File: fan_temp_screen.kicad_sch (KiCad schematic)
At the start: 19 parts, among them CN4 4P JST ZH, CN5 4P JST ZH, CN6 4P JST ZH

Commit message: Updated library name, updated and verified all footprints
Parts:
- C21: symbol EASYEDA2KICAD:C_100pF_C0G_0805 -> LiveAstra:C_100pF_C0G_0805
- CN4, CN5, CN6: symbol EASYEDA2KICAD:JST_ZH_4PIN_1A_50V -> LiveAstra:JST_ZH_4PIN_1A_50V
- R23, R24, R28, R30: symbol EASYEDA2KICAD:R_5k1Ohm_0402_62mW -> LiveAstra:R_5k1Ohm_0402_62mW
- R25, R26: symbol EASYEDA2KICAD:R_0Ohm_0805_125mW -> LiveAstra:R_0Ohm_0805_125mW
- R27: symbol EASYEDA2KICAD:R_10kOhm_0402_62mW -> LiveAstra:R_10kOhm_0402_62mW
- R29: symbol EASYEDA2KICAD:R_3k3Ohm_0805_125mW -> LiveAstra:R_3k3Ohm_0805_125mW
- TP48, TP49, TP50, TP51, TP52, TP53, TP54: symbol EASYEDA2KICAD:TestPoint_Thimble -> LiveAstra:TestPoint_Thimble
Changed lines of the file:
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@@
 	)
 	(symbol
-		(lib_id "EASYEDA2KICAD:TestPoint_Thimble")
+		(lib_id "LiveAstra:TestPoint_Thimble")
 		(at 187.96 96.52 0)
 		(unit 1)
@@
 	)
 	(symbol
-		(lib_id "EASYEDA2KICAD:TestPoint_Thimble")
+		(lib_id "LiveAstra:TestPoint_Thimble")
 		(at 142.24 40.64 0)
 		(unit 1)
@@
 	)
 	(symbol
-		(lib_id "EASYEDA2KICAD:R_0Ohm_0805_125mW")
+		(lib_id "LiveAstra:R_0Ohm_0805_125mW")
 		(at 167.64 48.26 0)
 		(unit 1)
@@
 	)
 	(symbol
-		(lib_id "EASYEDA2KICAD:JST_ZH_4PIN_1A_50V")
+		(lib_id "LiveAstra:JST_ZH_4PIN_1A_50V")
 		(at 106.68 152.4 180)
 		(unit 1)
@@
 	)
 	(symbol
-		(lib_id "EASYEDA2KICAD:R_5k1Ohm_0402_62mW")
+		(lib_id "LiveAstra:R_5k1Ohm_0402_62mW")
 		(at 124.46 86.36 90)
 		(unit 1)
@@
 	)
 	(symbol
-		(lib_id "EASYEDA2KICAD:+5V_IN")
+		(lib_id "LiveAstra:+5V_IN")
 		(at 132.08 60.96 0)
 		(unit 1)
@@
 	)
 	(symbol
-		(lib_id "EASYEDA2KICAD:C_100pF_C0G_0805")
+		(lib_id "LiveAstra:C_100pF_C0G_0805")
 		(at 215.9 55.88 90)
 		(unit 1)
@@
 	)
 	(symbol
-		(lib_id "EASYEDA2KICAD:R_10kOhm_0402_62mW")
+		(lib_id "LiveAstra:R_10kOhm_0402_62mW")
 		(at 177.8 40.64 90)
 		(unit 1)
@@
 	)
 	(symbol
-		(lib_id "EASYEDA2KICAD:TestPoint_Thimble")
+		(lib_id "LiveAstra:TestPoint_Thimble")
 		(at 144.78 142.24 0)
 		(unit 1)
@@
 	)
 	(symbol
-		(lib_id "EASYEDA2KICAD:TestPoint_Thimble")
+		(lib_id "LiveAstra:TestPoint_Thimble")
 		(at 157.48 35.56 0)
 		(unit 1)
@@
 	)
 	(symbol
-		(lib_id "EASYEDA2KICAD:R_5k1Ohm_0402_62mW")
+		(lib_id "LiveAstra:R_5k1Ohm_0402_62mW")
 		(at 203.2 142.24 90)
 		(unit 1)
@@
 	)
 	(symbol
-		(lib_id "EASYEDA2KICAD:TestPoint_Thimble")
+		(lib_id "LiveAstra:TestPoint_Thimble")
 		(at 228.6 45.72 0)
 		(unit 1)
@@
 	)
 	(symbol
-		(lib_id "EASYEDA2KICAD:TestPoint_Thimble")
+		(lib_id "LiveAstra:TestPoint_Thimble")
 		(at 149.86 91.44 0)
 		(unit 1)
@@
 	)
 	(symbol
-		(lib_id "EASYEDA2KICAD:R_3k3Ohm_0805_125mW")
+		(lib_id "LiveAstra:R_3k3Ohm_0805_125mW")
 		(at 205.74 48.26 0)
 		(unit 1)
@@
 	)
 	(symbol
-		(lib_id "EASYEDA2KICAD:JST_ZH_4PIN_1A_50V")
+		(lib_id "LiveAstra:JST_ZH_4PIN_1A_50V")
 		(at 106.68 101.6 180)
 		(unit 1)
@@
 	)
 	(symbol
-		(lib_id "EASYEDA2KICAD:R_0Ohm_0805_125mW")
+		(lib_id "LiveAstra:R_0Ohm_0805_125mW")
 		(at 134.62 43.18 0)
 		(unit 1)
@@
 	)
 	(symbol
-		(lib_id "EASYEDA2KICAD:R_5k1Ohm_0402_62mW")
+		(lib_id "LiveAstra:R_5k1Ohm_0402_62mW")
 		(at 124.46 137.16 90)
 		(unit 1)
@@
 	)
 	(symbol
-		(lib_id "EASYEDA2KICAD:JST_ZH_4PIN_1A_50V")
+		(lib_id "LiveAstra:JST_ZH_4PIN_1A_50V")
 		(at 106.68 50.8 180)
 		(unit 1)
@@
 	)
 	(symbol
-		(lib_id "EASYEDA2KICAD:R_5k1Ohm_0402_62mW")
+		(lib_id "LiveAstra:R_5k1Ohm_0402_62mW")
 		(at 213.36 91.44 90)
 		(unit 1)
@@
 	)
 	(symbol
-		(lib_id "EASYEDA2KICAD:TestPoint_Thimble")
+		(lib_id "LiveAstra:TestPoint_Thimble")
 		(at 177.8 147.32 0)
 		(unit 1)

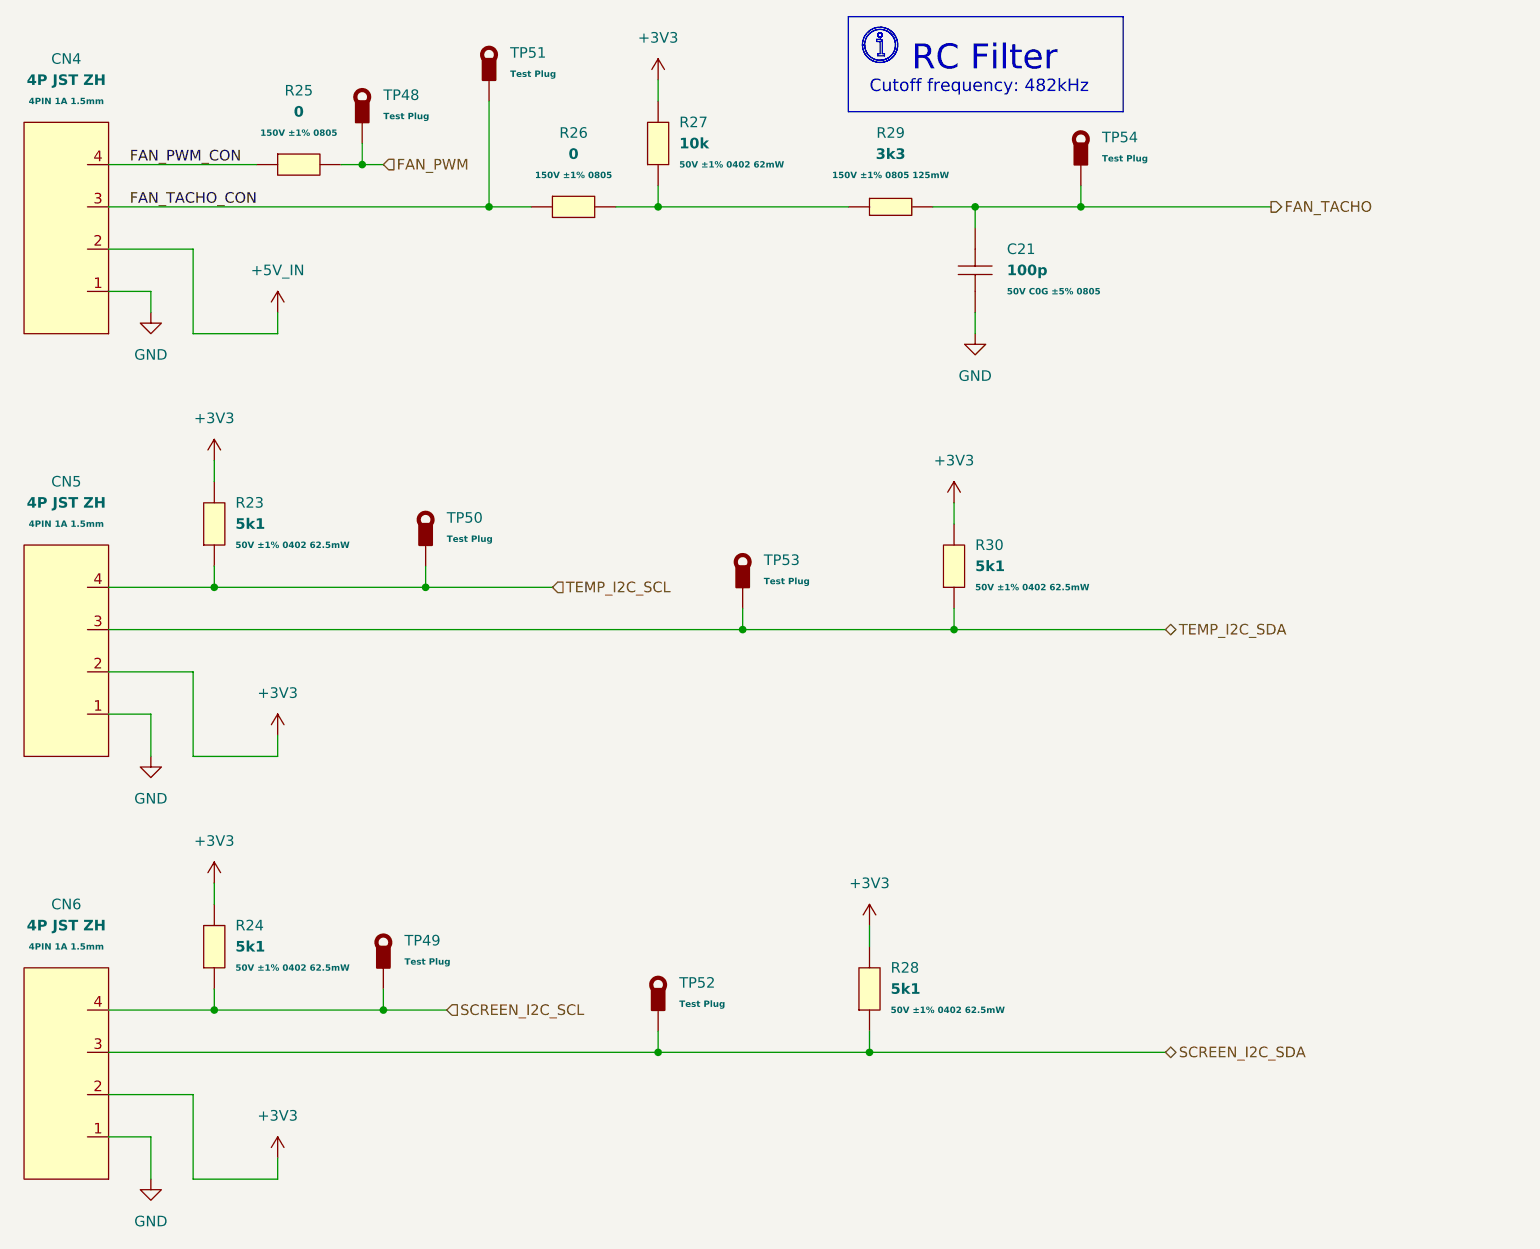
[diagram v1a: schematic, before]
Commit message: Finished layout no drc or erc errors
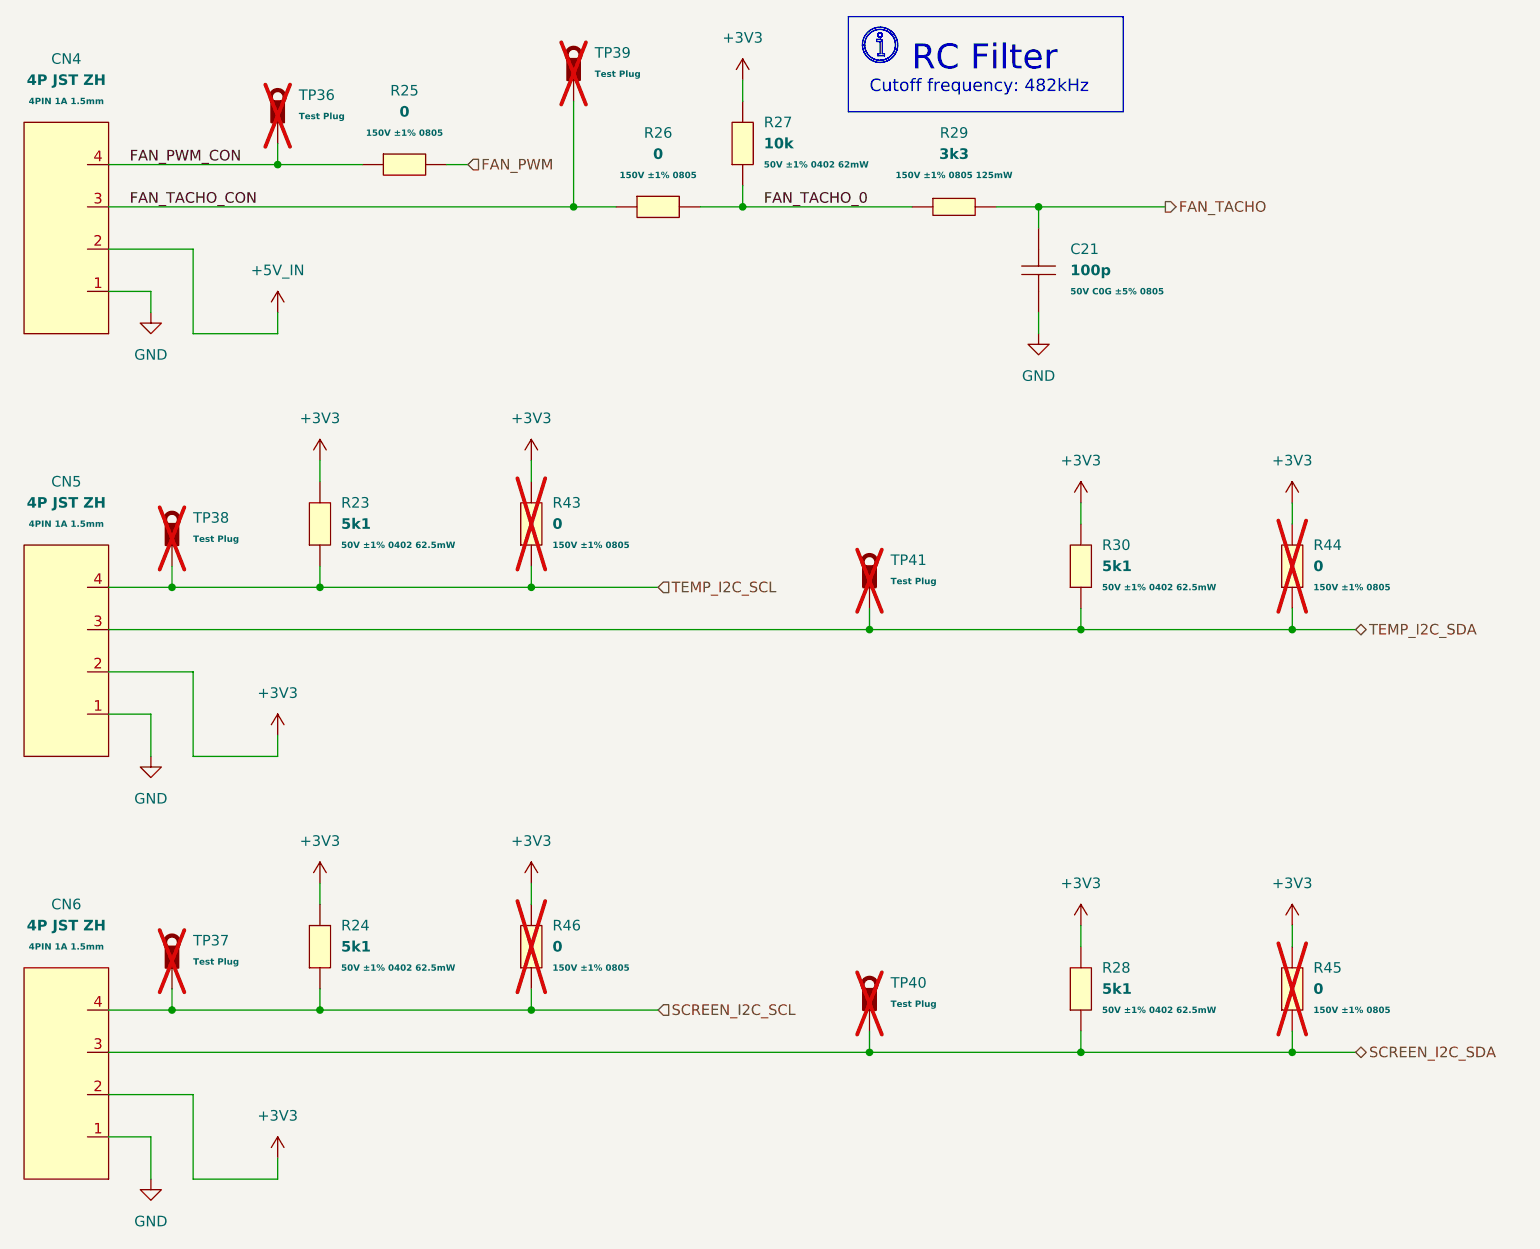
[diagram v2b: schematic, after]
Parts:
- removed TP54: TestPoint_Thimble, TestPoint:TestPoint_Loop_D3.50mm_Drill0.9mm_Beaded, symbol LiveAstra:TestPoint_Thimble
- added R43, R44, R45, R46: 0, LiveAstra:R_0805_2012Metric_Pad1.20x1.40mm_HandSolder, symbol LiveAstra:R_0Ohm_0805_125mW
- C21: footprint Capacitor_SMD:C_0805_2012Metric_Pad1.18x1.45mm_HandSolder -> LiveAstra:C_0805_2012Metric_Pad1.18x1.45mm_HandSolder
- CN4, CN5, CN6: footprint Connector_JST:JST_ZH_B4B-ZR_1x04_P1.50mm_Vertical -> LiveAstra:JST_ZH_B4B-ZR_1x04_P1.50mm_Vertical
- R23, R24, R27, R28, R30: footprint Resistor_SMD:R_0402_1005Metric -> LiveAstra:R_0402_1005Metric
- R25, R26, R29: footprint Resistor_SMD:R_0805_2012Metric_Pad1.20x1.40mm_HandSolder -> LiveAstra:R_0805_2012Metric_Pad1.20x1.40mm_HandSolder
- TP36: renamed from TP48; footprint TestPoint:TestPoint_Loop_D3.50mm_Drill0.9mm_Beaded -> LiveAstra:TestPoint_Loop_D3.50mm_Drill0.9mm_Beaded; now not fitted; now left out of the parts list
- TP37: renamed from TP49; footprint TestPoint:TestPoint_Loop_D3.50mm_Drill0.9mm_Beaded -> LiveAstra:TestPoint_Loop_D3.50mm_Drill0.9mm_Beaded; now not fitted; now left out of the parts list
- TP38: renamed from TP50; footprint TestPoint:TestPoint_Loop_D3.50mm_Drill0.9mm_Beaded -> LiveAstra:TestPoint_Loop_D3.50mm_Drill0.9mm_Beaded; now not fitted; now left out of the parts list
- TP39: renamed from TP51; footprint TestPoint:TestPoint_Loop_D3.50mm_Drill0.9mm_Beaded -> LiveAstra:TestPoint_Loop_D3.50mm_Drill0.9mm_Beaded; now not fitted; now left out of the parts list
- TP40: renamed from TP52; footprint TestPoint:TestPoint_Loop_D3.50mm_Drill0.9mm_Beaded -> LiveAstra:TestPoint_Loop_D3.50mm_Drill0.9mm_Beaded; now not fitted; now left out of the parts list
- TP41: renamed from TP53; footprint TestPoint:TestPoint_Loop_D3.50mm_Drill0.9mm_Beaded -> LiveAstra:TestPoint_Loop_D3.50mm_Drill0.9mm_Beaded; now not fitted; now left out of the parts list
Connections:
- net +3V3: now also R43.2, R44.2, R45.2, R46.2
- net FAN_PWM: no longer TP36.1
- net FAN_PWM_CON: now also TP36.1
- net SCREEN_I2C_SCL: now also R46.1
- net SCREEN_I2C_SDA: now also R45.1
- net TEMP_I2C_SCL: now also R43.1
- net TEMP_I2C_SDA: now also R44.1
- net FAN_TACHO_0: now reaches R26.2, R27.1, R29.1
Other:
- moved on the sheet: C21, R23, R24, R25, R26, R27, R28, R29, R30

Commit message: Work on kibot
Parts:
- CN4, CN5, CN6: Extra Values 4PIN 1A 1.5mm -> 4PIN 1A 1.5mm
- R23, R24, R28, R30: Extra Values 50V ±1% 0402 62.5mW -> 50V ±1% 0402 62.5mW
- R29: Extra Values 150V ±1% 0805 125mW -> 150V ±1% 0805 125mW

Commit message: workflow
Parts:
- TP36, TP37, TP38, TP39, TP40, TP41: now fitted
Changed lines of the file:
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@@
 		(in_bom no)
 		(on_board yes)
-		(dnp yes)
+		(dnp no)
 		(fields_autoplaced yes)
 		(property "Reference" "TP41"
@@
 			)
 		)
+		(property "Extra Value" ""
+			(at 203.2 96.52 0)
+			(effects
+				(font
+					(size 1.27 1.27)
+				)
+				(hide yes)
+			)
+		)
 		(pin "1"
 		)
@@
 		(in_bom no)
 		(on_board yes)
-		(dnp yes)
+		(dnp no)
 		(fields_autoplaced yes)
 		(property "Reference" "TP36"
@@
 			)
 		)
+		(property "Extra Value" ""
+			(at 132.08 40.64 0)
+			(effects
+				(font
+					(size 1.27 1.27)
+				)
+				(hide yes)
+			)
+		)
 		(pin "1"
 		)
@@
 			)
 		)
+		(property "Extra Value" ""
+			(at 177.8 48.26 0)
+			(effects
+				(font
+					(size 1.27 1.27)
+				)
+				(hide yes)
+			)
+		)
 		(pin "1"
 		)
@@
 			)
 		)
+		(property "Extra Value" ""
+			(at 106.68 152.4 0)
+			(effects
+				(font
+					(size 1.27 1.27)
+				)
+				(hide yes)
+			)
+		)
 		(pin "1"
 		)
@@
 			)
 		)
+		(property "Extra Value" ""
+			(at 137.16 86.36 0)
+			(effects
+				(font
+					(size 1.27 1.27)
+				)
+				(hide yes)
+			)
+		)
 		(pin "1"
 		)
@@
 			)
 		)
+		(property "Extra Value" ""
+			(at 223.52 55.88 0)
+			(effects
+				(font
+					(size 1.27 1.27)
+				)
+				(hide yes)
+			)
+		)
 		(pin "1"
 		)
@@
 			)
 		)
+		(property "Extra Value" ""
+			(at 187.96 40.64 0)
+			(effects
+				(font
+					(size 1.27 1.27)
+				)
+				(hide yes)
+			)
+		)
 		(pin "2"
 		)
@@
 		(in_bom no)
 		(on_board yes)
-		(dnp yes)
+		(dnp no)
 		(fields_autoplaced yes)
 		(property "Reference" "TP37"
@@
 			)
 		)
+		(property "Extra Value" ""
+			(at 119.38 142.24 0)
+			(effects
+				(font
+					(size 1.27 1.27)
+				)
+				(hide yes)
+			)
+		)
 		(pin "1"
 		)
@@
 		(in_bom no)
 		(on_board yes)
-		(dnp yes)
+		(dnp no)
 		(fields_autoplaced yes)
 		(property "Reference" "TP39"
@@
 			)
 		)
+		(property "Extra Value" ""
+			(at 167.64 35.56 0)
+			(effects
+				(font
+					(size 1.27 1.27)
+				)
+				(hide yes)
+			)
+		)
 		(pin "1"
 		)
@@
 			)
 		)
+		(property "Extra Value" ""
+			(at 228.6 142.24 0)
+			(effects
+				(font
+					(size 1.27 1.27)
+				)
+				(hide yes)
+			)
+		)
 		(pin "1"
 		)
@@
 			)
 		)
+		(property "Extra Value" ""
+			(at 254 142.24 0)
+			(effects
+				(font
+					(size 1.27 1.27)
+				)
+				(hide yes)
+			)
+		)
 		(pin "1"
 		)
@@
 		(in_bom no)
 		(on_board yes)
-		(dnp yes)
+		(dnp no)
 		(fields_autoplaced yes)
 		(property "Reference" "TP38"
@@
 			)
 		)
+		(property "Extra Value" ""
+			(at 119.38 91.44 0)
+			(effects
+				(font
+					(size 1.27 1.27)
+				)
+				(hide yes)
+			)
+		)
 		(pin "1"
 		)
@@
 			)
 		)
+		(property "Extra Value" ""
+			(at 213.36 48.26 0)
+			(effects
+				(font
+					(size 1.27 1.27)
+				)
+				(hide yes)
+			)
+		)
 		(pin "2"
 		)
@@
 			)
 		)
+		(property "Extra Value" ""
+			(at 106.68 101.6 0)
+			(effects
+				(font
+					(size 1.27 1.27)
+				)
+				(hide yes)
+			)
+		)
 		(pin "1"
 		)
@@
 			)
 		)
+		(property "Extra Value" ""
+			(at 147.32 43.18 0)
+			(effects
+				(font
+					(size 1.27 1.27)
+				)
+				(hide yes)
+			)
+		)
 		(pin "1"
 		)
@@
 			)
 		)
+		(property "Extra Value" ""
+			(at 137.16 137.16 0)
+			(effects
+				(font
+					(size 1.27 1.27)
+				)
+				(hide yes)
+			)
+		)
 		(pin "1"
 		)
@@
 			)
 		)
+		(property "Extra Value" ""
+			(at 254 91.44 0)
+			(effects
+				(font
+					(size 1.27 1.27)
+				)
+				(hide yes)
+			)
+		)
 		(pin "1"
 		)
@@
 			)
 		)
+		(property "Extra Value" ""
+			(at 162.56 137.16 0)
+			(effects
+				(font
+					(size 1.27 1.27)
+				)
+				(hide yes)
+			)
+		)
 		(pin "1"
 		)
@@
 			)
 		)
+		(property "Extra Value" ""
+			(at 162.56 86.36 0)
+			(effects
+				(font
+					(size 1.27 1.27)
+				)
+				(hide yes)
+			)
+		)
 		(pin "1"
 		)
@@
 			)
 		)
+		(property "Extra Value" ""
+			(at 106.68 50.8 0)
+			(effects
+				(font
+					(size 1.27 1.27)
+				)
+				(hide yes)
+			)
+		)
 		(pin "1"
 		)
@@
 			)
 		)
+		(property "Extra Value" ""
+			(at 228.6 91.44 0)
+			(effects
+				(font
+					(size 1.27 1.27)
+				)
+				(hide yes)
+			)
+		)
 		(pin "1"
 		)
@@
 		(in_bom no)
 		(on_board yes)
-		(dnp yes)
+		(dnp no)
 		(fields_autoplaced yes)
 		(property "Reference" "TP40"
@@
 			)
 		)
+		(property "Extra Value" ""
+			(at 203.2 147.32 0)
+			(effects
+				(font
+					(size 1.27 1.27)
+				)
+				(hide yes)
+			)
+		)

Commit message: workflow
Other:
- title: (none) -> Fan, Temperature and Screen
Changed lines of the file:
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@@
 	(generator_version "8.0")
 	(paper "A4")
+	(title_block
+		(title "Fan, Temperature and Screen")
+	)
 	(junction
 		(at 228.6 99.06)
